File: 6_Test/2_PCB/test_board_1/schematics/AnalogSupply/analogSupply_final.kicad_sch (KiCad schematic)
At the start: 19 parts, among them U3 ADA4807-1AKSZ-R7

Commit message: analog final complete
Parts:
- removed V--1: 0, symbol Simulation_SPICE:VDC
- removed V?: 3, symbol Simulation_SPICE:VDC
- R3: value RC0402FR-074K7L -> ${SIM.PARAMS}
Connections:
- net AVDD: now also C7.2; no longer C4.2
- net GND: now also C7.1, U3.2 (-VS), U?.2 (-VS); no longer C4.1
- net VHI: now also C4.2; no longer C7.2
- net VLO: now also C4.1; no longer C7.1
- net Analog_Discover_Input: now reaches C3.1, L?.2

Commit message: progress on merging
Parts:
- removed C? (x2): CL10A475KP8NNNC, CAP_0603_CL10A_1P6XP8_SAM, symbol Cap4.7uF:CL10A475KP8NNNC
- removed L?: BLM18PG121SN1D, IND_BLM18_0603_MUR, symbol ferriteBeads120Ohm:BLM18PG121SN1D
- removed R7: 3310Y-001-103L, 3310Y-001-103L:TRIM_3310Y-001-103L, symbol potentiometer:3310Y-001-103L
- removed R?: RC0402JR-071KL, RC0402N_YAG, symbol Resistor1k:RC0402JR-071KL
- removed U?: TPS74501PDRVR, DRV0006A, symbol LDO:TPS74501PDRVR
- removed U?: ADA4807-1AKSZ-R7, KS-6_ADI, symbol Opamp:ADA4807-1AKSZ-R7
- added C1, C2: CL10A475KP8NNNC, CAP_0603_CL10A_1P6XP8_SAM, symbol Cap4.7uF:CL10A475KP8NNNC
- added L1: BLM18PG121SN1D, IND_BLM18_0603_MUR, symbol ferriteBeads120Ohm:BLM18PG121SN1D
- added R1: RC0402JR-071KL, RC0402N_YAG, symbol Resistor1k:RC0402JR-071KL
- added R6: 3310Y-001-103L, 3310Y-001-103L:TRIM_3310Y-001-103L, symbol potentiometer:3310Y-001-103L
- added U1: TPS74501PDRVR, DRV0006A, symbol LDO:TPS74501PDRVR
- added U2: ADA4807-1AKSZ-R7, KS-6_ADI, symbol Opamp:ADA4807-1AKSZ-R7
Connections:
- net Analog_Discover_Input is gone; now on net AVDD: C3.1
- net AVDD: now also R1.1, U1.1 (OUT)
- net GND: now also C1.2, C2.2, U1.3 (GND), U1.7 (PAD), U2.2 (-VS); no longer C3.2, C5.1, C6.1, C7.1, R3.1, R5.2
- net VHI: now also U2.1 (VOUT), U2.4 (-IN)
- net at R4.2: now also R5.1, U2.3 (+IN); no longer R2.1
- net at R3.2: now also R2.2, U1.2 (FB)
- net at U3.5 (*DISABLE), U3.6 (+VS): now also C2.1, L1.1, U1.4 (EN), U1.6 (IN), U2.5 (*DISABLE), U2.6 (+VS)
- new net: R1.2, R2.1
- new net: R5.2, R6.1, U3.3 (+IN)
- new net AVSS: C3.2, C5.1, C6.1, C7.1, R3.1, R6.2
- new net VSUP: C1.1, L1.2
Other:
- note added: "The ADC connects AVSS to GND. This jumper should only be connected for simulations"

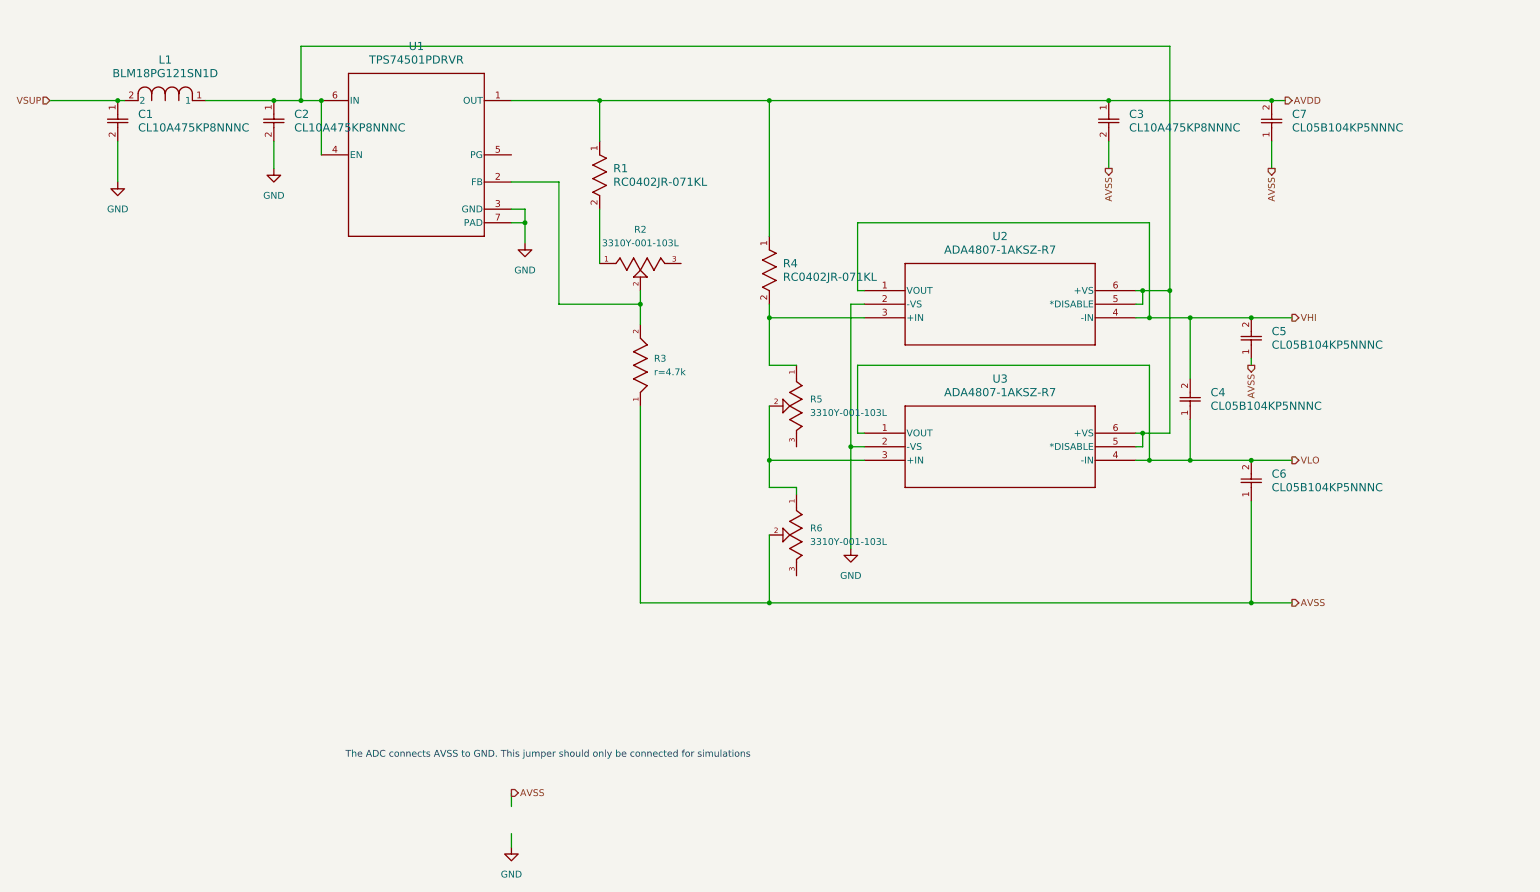
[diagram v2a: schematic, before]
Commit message: fixed digital supply, added three sheets to board main
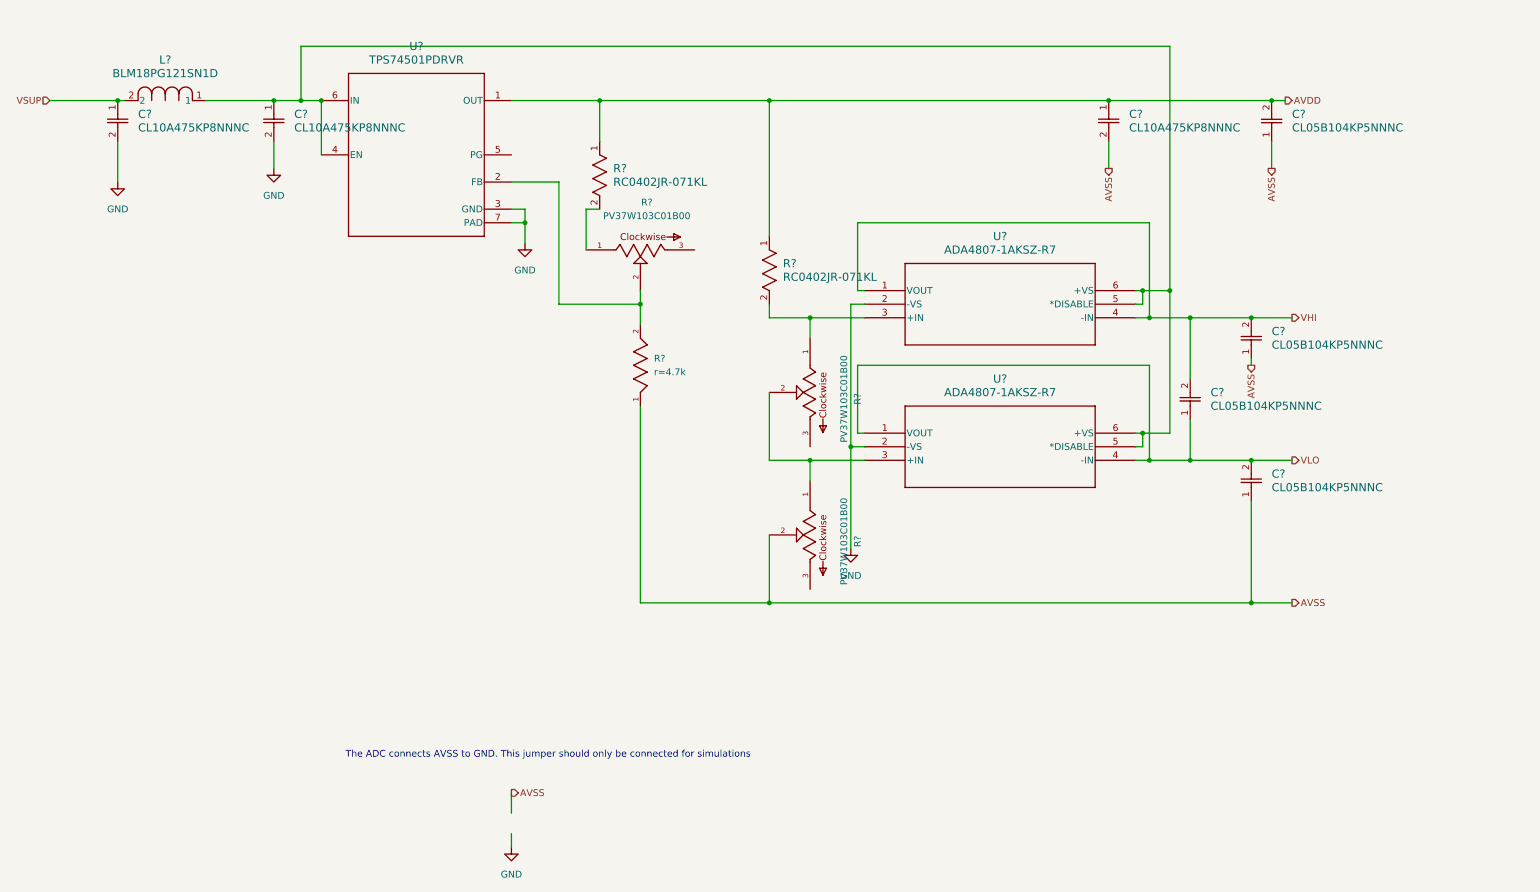
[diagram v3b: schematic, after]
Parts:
- removed R2, R5, R6: 3310Y-001-103L, 3310Y-001-103L:TRIM_3310Y-001-103L, symbol potentiometer:3310Y-001-103L
- added R? (x3): PV37W103C01B00, PV37W103C01B00:TRIM_PV37W103C01B00, symbol pot_10turn:PV37W103C01B00
- renumbered C5 to C?, C7 to C?, C4 to C?, C6 to C?, C2 to C?, C3 to C?, C1 to C?, L1 to L?, R4 to R?, R1 to R?, R3 to R?, U3 to U?, U1 to U?, U2 to U?
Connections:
- net AVSS: now also R?.2
- net at R?.2, U?.3 (+IN): now also R?.1
- net at R?.2: now also R?.1
- net at R?.2, U?.2 (FB): now also R?.2
- net at U?.3 (+IN): now also R?.1, R?.2

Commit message: final draft of board done.
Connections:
- net VA: now reaches C?.1, L?.1, U?.4 (EN), U?.5 (*DISABLE), U?.5 (*DISABLE), U?.6 (+VS), U?.6 (+VS), U?.6 (IN)
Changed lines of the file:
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@@
 	)
 	(junction
+		(at 72.39 44.45)
+		(diameter 0)
+		(color 0 0 0 0)
+	)
+	(junction
 		(at 252.73 44.45)
 		(diameter 0)
@@
 	(wire
 		(pts
-			(xy 71.12 44.45) (xy 74.93 44.45)
+			(xy 71.12 44.45) (xy 72.39 44.45)
 		)
 		(stroke
@@
 	(wire
 		(pts
+			(xy 72.39 44.45) (xy 72.39 76.2)
+		)
+		(stroke
+			(width 0)
+			(type default)
+		)
+	)
+	(wire
+		(pts
 			(xy 127 64.77) (xy 124.46 64.77)
 		)
@@
 		)
 	)
+	(wire
+		(pts
+			(xy 72.39 44.45) (xy 74.93 44.45)
+		)
+		(stroke
+			(width 0)
+			(type default)
+		)
+	)
 	(text "The ADC connects AVSS to GND. This jumper should only be connected for simulations"
 		(exclude_from_sim no)
@@
 		)
 	)
+	(hierarchical_label "VA"
+		(shape output)
+		(at 72.39 76.2 270)
+		(fields_autoplaced yes)
+		(effects
+			(font
+				(size 1.27 1.27)
+			)
+			(justify right)
+		)
+	)
 	(hierarchical_label "AVSS"
 		(shape output)
@@
 			(project "board_main_sim"
 				(path "/9c0580c5-7bd5-4e54-bf4c-826aa4ac3630/0a919f49-2db5-4a49-acae-598537b168fb"
-					(reference "#PWR05")
+					(reference "#PWR07")
 					(unit 1)
 				)
@@
 			(project "board_main_sim"
 				(path "/9c0580c5-7bd5-4e54-bf4c-826aa4ac3630/0a919f49-2db5-4a49-acae-598537b168fb"
-					(reference "#PWR04")
+					(reference "#PWR06")
 					(unit 1)
 				)
@@
 			(project "board_main_sim"
 				(path "/9c0580c5-7bd5-4e54-bf4c-826aa4ac3630/0a919f49-2db5-4a49-acae-598537b168fb"
-					(reference "#PWR07")
+					(reference "#PWR09")
 					(unit 1)
 				)
@@
 			(project "board_main_sim"
 				(path "/9c0580c5-7bd5-4e54-bf4c-826aa4ac3630/0a919f49-2db5-4a49-acae-598537b168fb"
-					(reference "#PWR06")
+					(reference "#PWR08")
 					(unit 1)
 				)
@@
 			(project "board_main_sim"
 				(path "/9c0580c5-7bd5-4e54-bf4c-826aa4ac3630/0a919f49-2db5-4a49-acae-598537b168fb"
-					(reference "#PWR03")
+					(reference "#PWR05")
 					(unit 1)
 				)
